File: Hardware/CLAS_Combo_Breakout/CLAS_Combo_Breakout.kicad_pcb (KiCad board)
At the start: 4 copper layers, 60 x 60 mm, 87 parts, among them J1 USB_C_Receptacle_USB2.0, J2 ZED, J3 NEO, J4 USB_C_Receptacle_USB2.0, J5 Conn_SMA, U1 USBLC6-2P6, U10 NT1191GEAE3S, U2 ZED-F9P, U3 NEO-D9C-00B, U4 USBLC6-2P6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

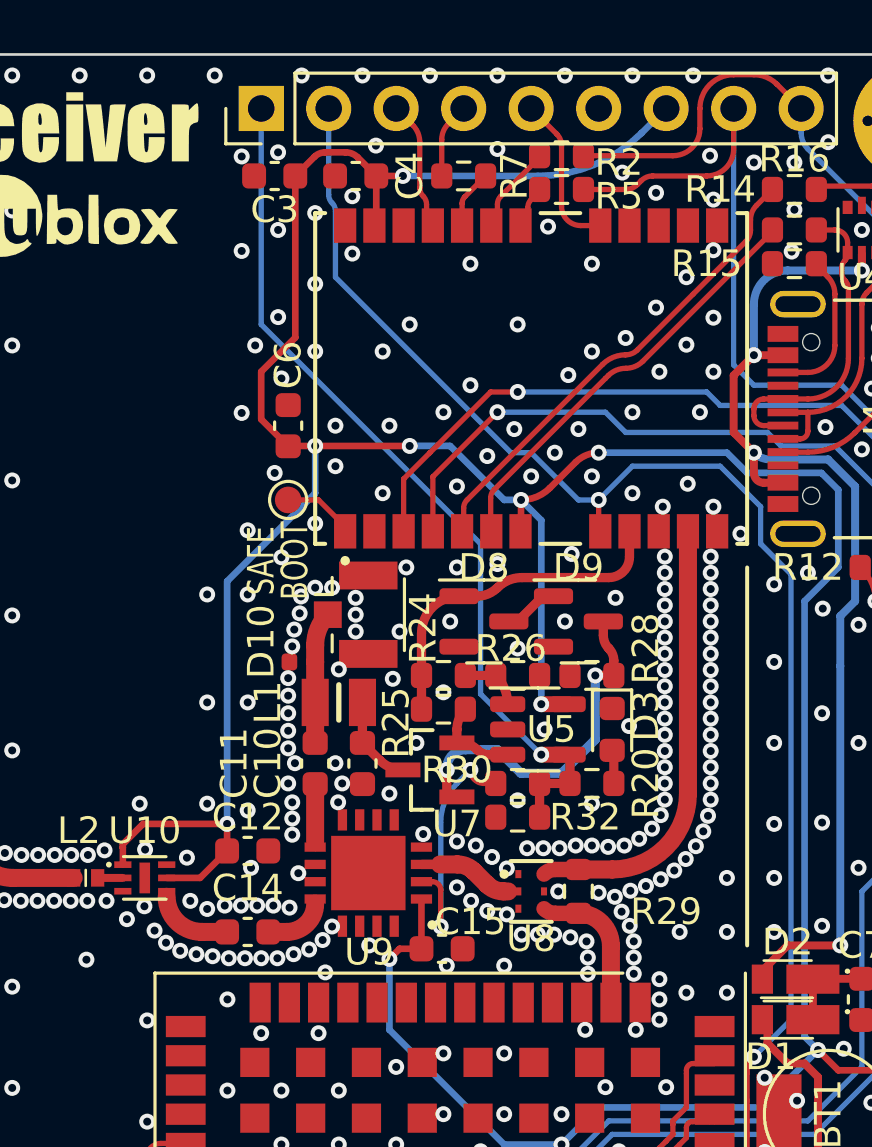
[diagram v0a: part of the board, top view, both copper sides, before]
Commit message: プルダウンRをプルアップRに変更、EANTのLEDを移動
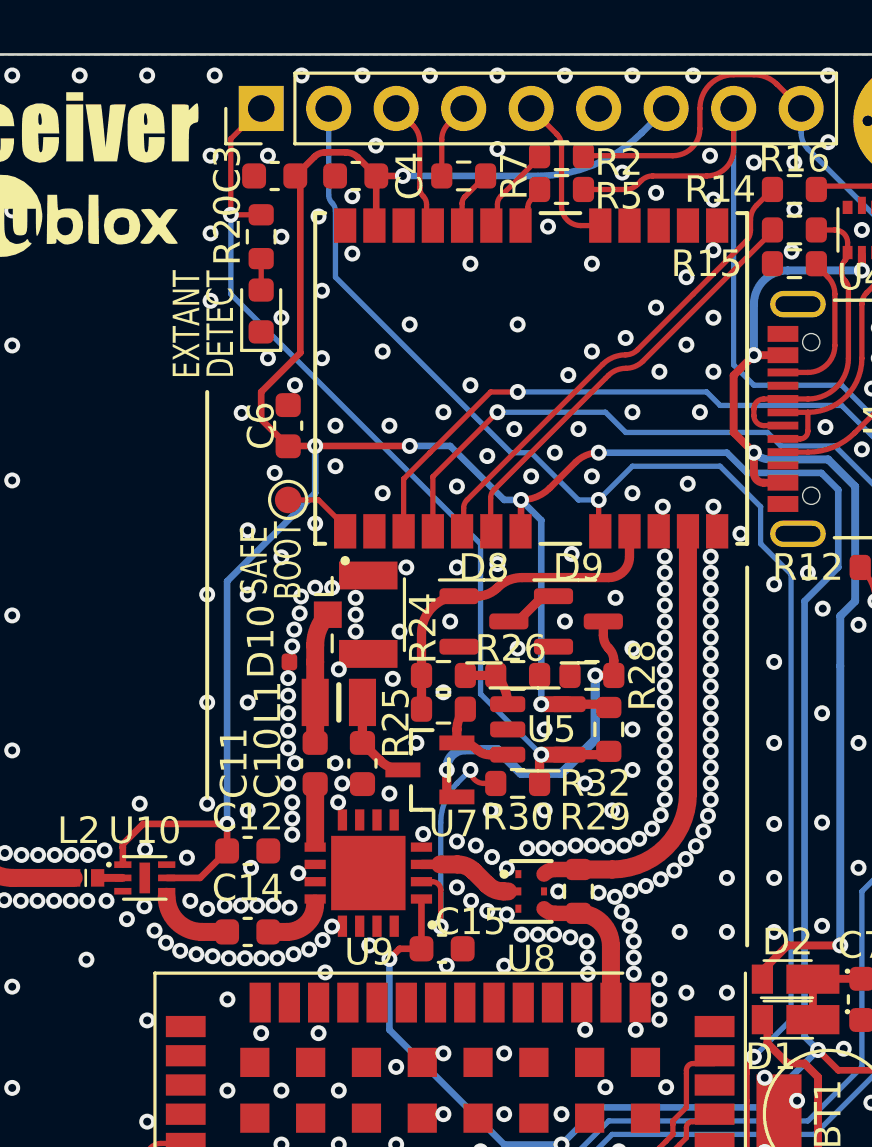
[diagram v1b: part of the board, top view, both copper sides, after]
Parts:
- moved R20 24.0 mm to (133.0, 96.9), turned to -90 degrees
- moved D3 20.6 mm to (133.0, 99.7), turned to 90 degrees
- moved R32 4.76 mm to (146.1, 115.4), turned to -90 degrees
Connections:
- R32 pad 1: GND -> +3.3V
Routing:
- net +3.3V: track 183.0 -> 184.8 mm
- net /EXTANT_DETECT: track 33.2 -> 34.5 mm, vias 1 -> 2
- net GND: vias 539 -> 544
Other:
- board text added: "DETECT"
- board text added: "EXTANT"

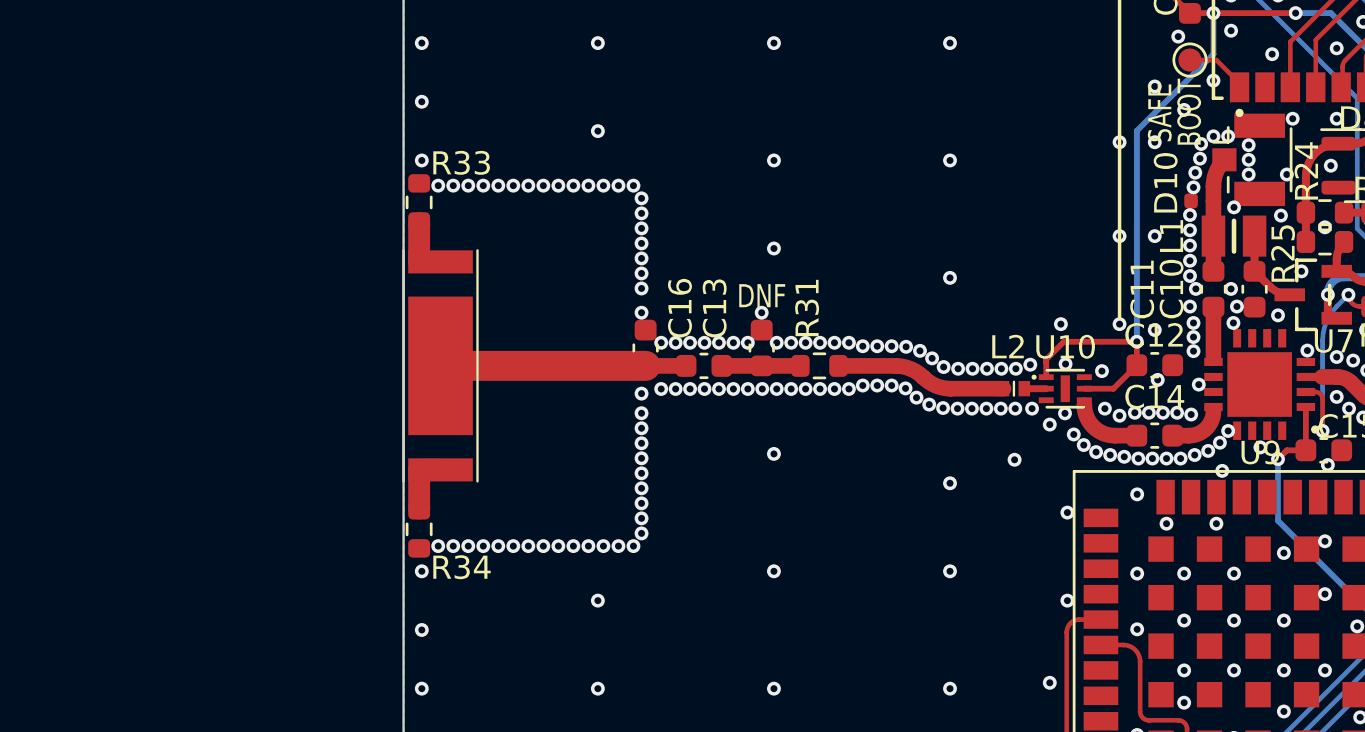
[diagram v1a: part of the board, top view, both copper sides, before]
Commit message: アンテナのFootprintをデータシートに準拠
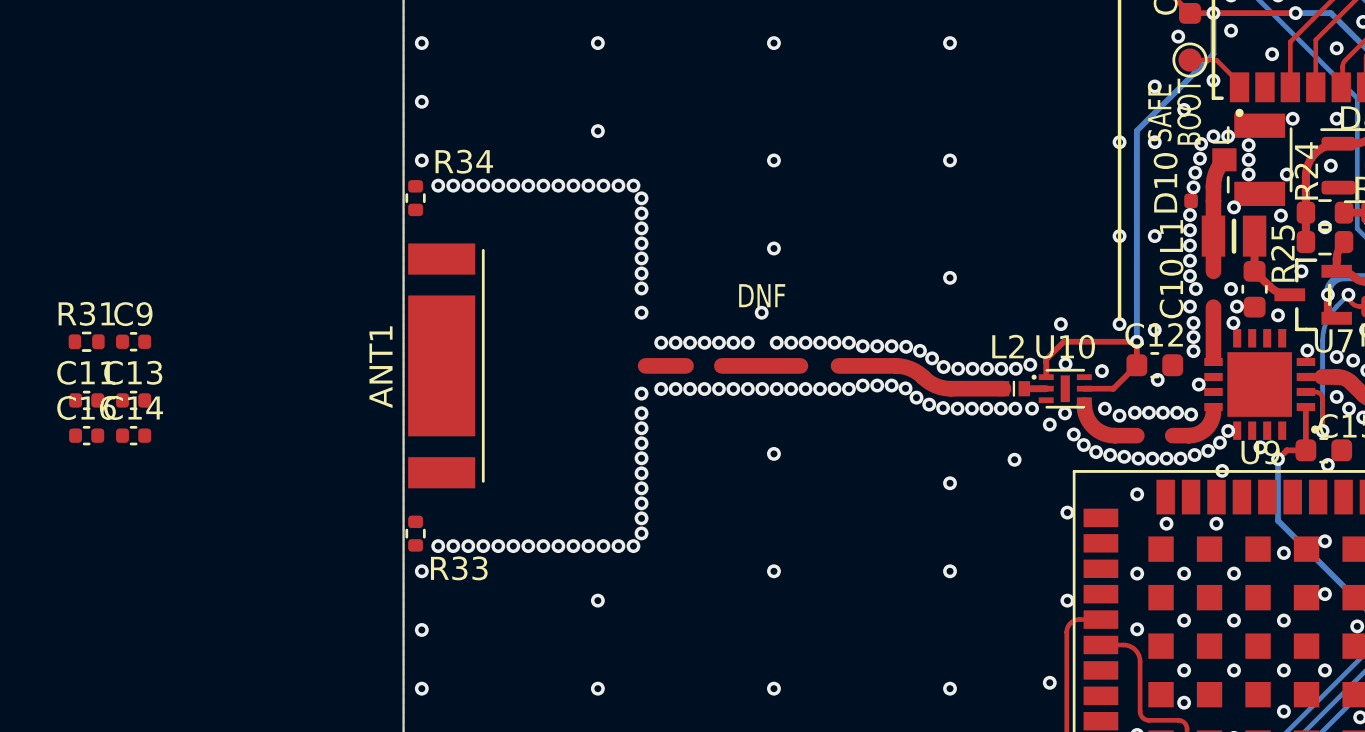
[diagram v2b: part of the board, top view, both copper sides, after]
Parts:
- ANT1: value GGBLA.125.A -> GGBLA125A
- C11, C13, C14, C16, C9: footprint Capacitor_SMD:C_0603_1608Metric -> Capacitor_SMD:C_0402_1005Metric
- R31, R33, R34: footprint Resistor_SMD:R_0603_1608Metric -> Resistor_SMD:R_0402_1005Metric
- moved C11 49.0 mm to (86.3, 121.5), turned to 0 degrees
- moved C14 44.2 mm to (88.3, 123.0), turned to 0 degrees
- moved R31 31.7 mm to (86.3, 119.0)
- moved C9 27.2 mm to (88.3, 119.0), turned to 0 degrees
- moved C13 24.7 mm to (88.3, 121.5)
- moved C16 24.5 mm to (86.3, 123.0), turned to 0 degrees
- moved R33 14.3 mm to (100.5, 127.3), turned to -90 degrees
- moved R34 14.3 mm to (100.5, 112.7), turned to 90 degrees
- moved ANT1 0.05 mm to (101.7, 120.0), turned to 90 degrees
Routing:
- net Net-(ANT1-Pad1): track 10.6 -> 1.75 mm
- net Net-(ANT1-Pad3): track 2.60 -> 0.00 mm
- net Net-(ANT1-Pad2): track 2.60 -> 0.00 mm

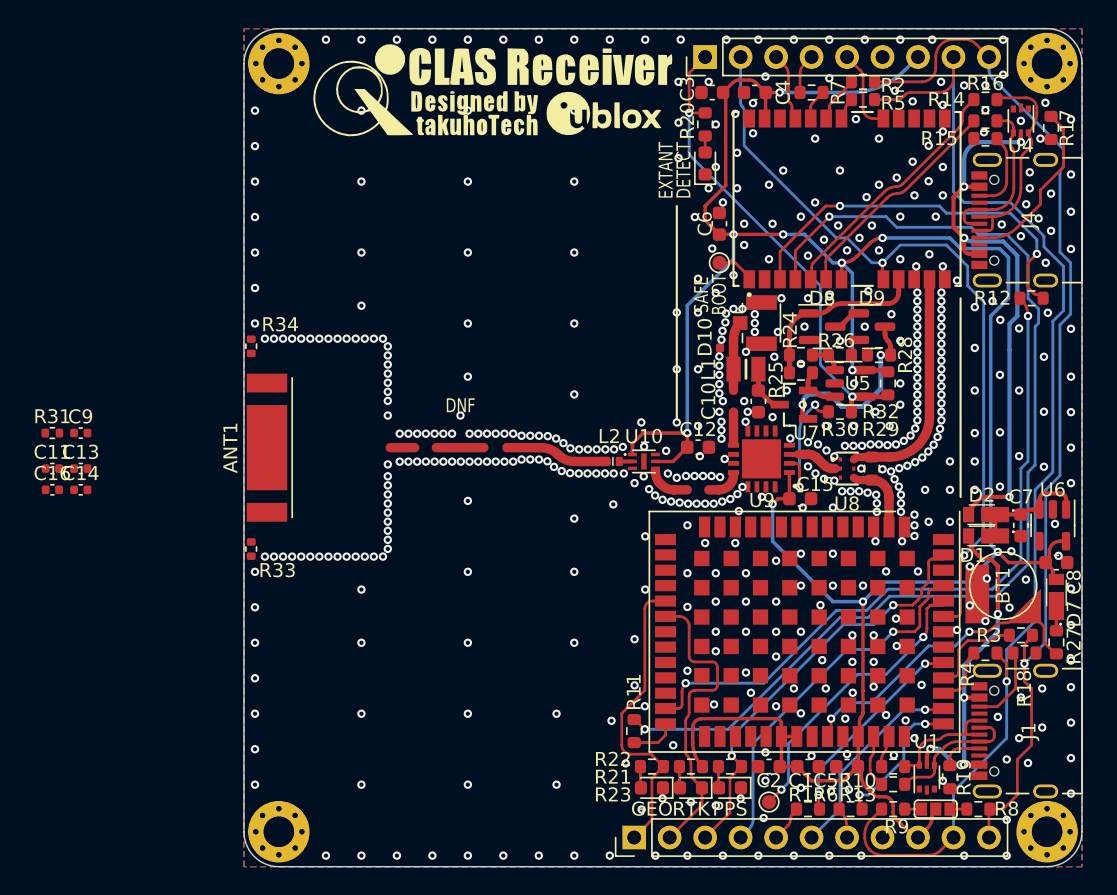
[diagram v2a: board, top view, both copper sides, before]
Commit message: トランジスタの記号をQに変更、REFを整理
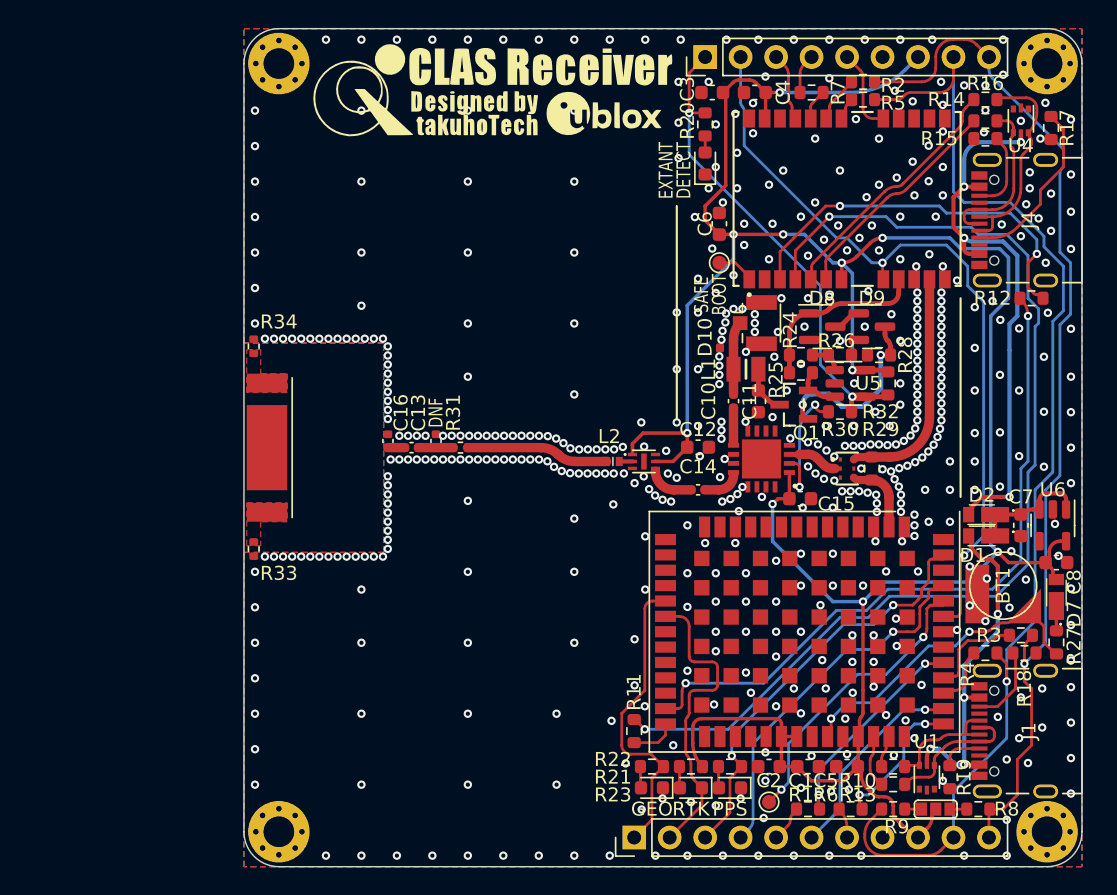
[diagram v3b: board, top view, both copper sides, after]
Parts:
- ANT1: value GGBLA125A -> GGBLA.125.A
- moved C11 49.0 mm to (135.1, 116.7), turned to -90 degrees
- moved C14 44.2 mm to (132.5, 123.0), turned to 180 degrees
- moved R31 29.2 mm to (115.5, 120.0)
- moved C9 25.4 mm to (113.8, 119.5), turned to 90 degrees
- moved C16 24.3 mm to (110.3, 119.5), turned to 90 degrees
- moved C13 23.7 mm to (112.0, 120.0)
- moved R33 0.18 mm to (100.7, 127.3)
- moved R34 0.18 mm to (100.7, 112.7)
- renumbered U7 to Q1, U10 to U7, U9 to U8, U8 to U9
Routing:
- net Net-(L2-Pad1): track 7.39 -> 10.2 mm
- net Net-(C13-Pad2): track 3.40 -> 2.51 mm
- net Net-(ANT1-Pad1): track 1.75 -> 1.21 mm
- net GND: vias 544 -> 530
- added copper zone on F.Cu, net Net-(ANT1-Pad2)
- added copper zone on F.Cu, net Net-(ANT1-Pad3)

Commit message: アンテナ伝送路0.678mmバージョン
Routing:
- net Net-(ANT1-Pad1): track 1.21 -> 9.87 mm
- net GND: vias 530 -> 548

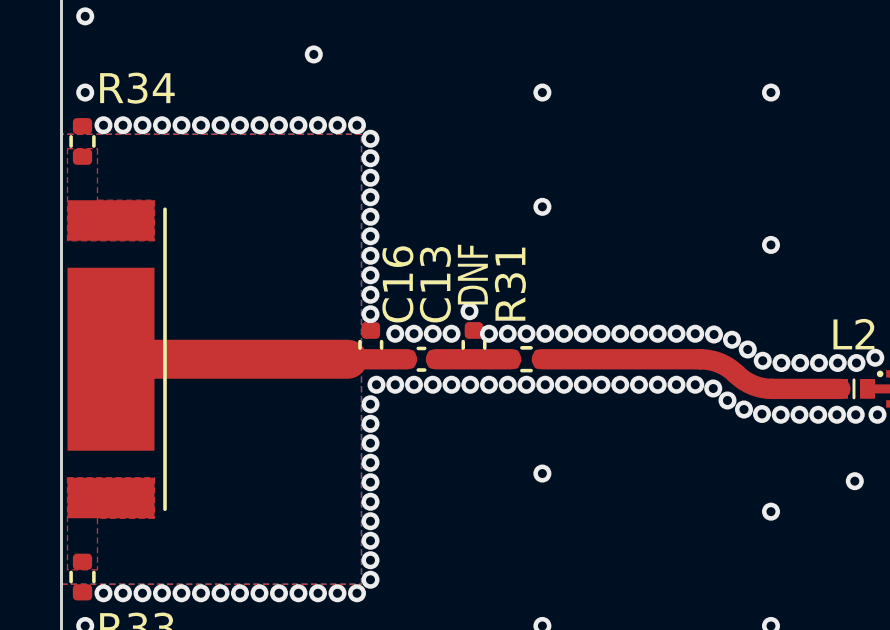
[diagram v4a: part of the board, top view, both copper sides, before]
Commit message: アンテナのマッチング回路を再設計
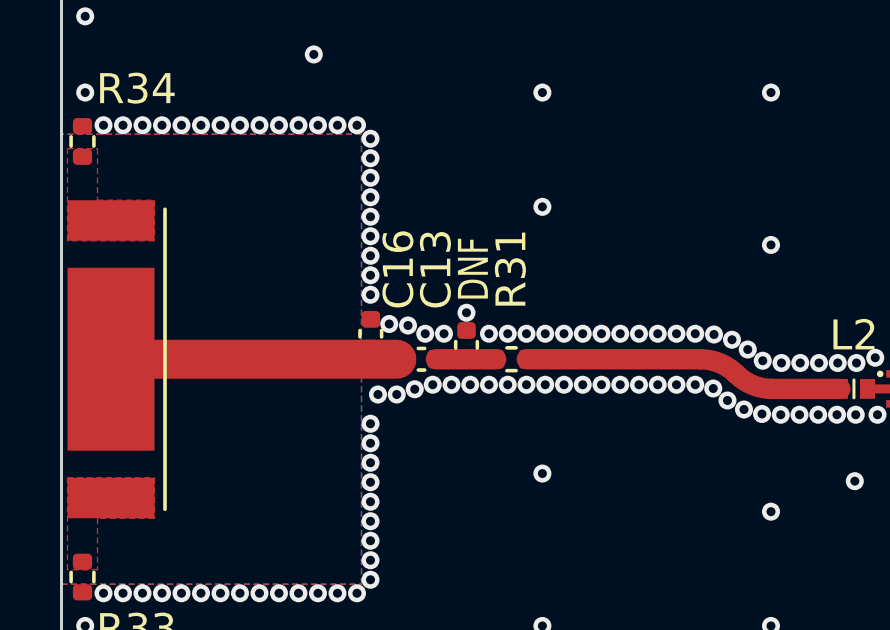
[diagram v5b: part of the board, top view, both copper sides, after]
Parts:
- moved R31 0.50 mm to (115.0, 120.0)
- moved C16 0.37 mm to (110.3, 119.2)
- moved C9 0.25 mm to (113.5, 119.5)
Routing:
- net Net-(L2-Pad1): track 10.2 -> 10.7 mm
- net Net-(C13-Pad2): track 2.51 -> 2.01 mm
- net GND: vias 548 -> 546

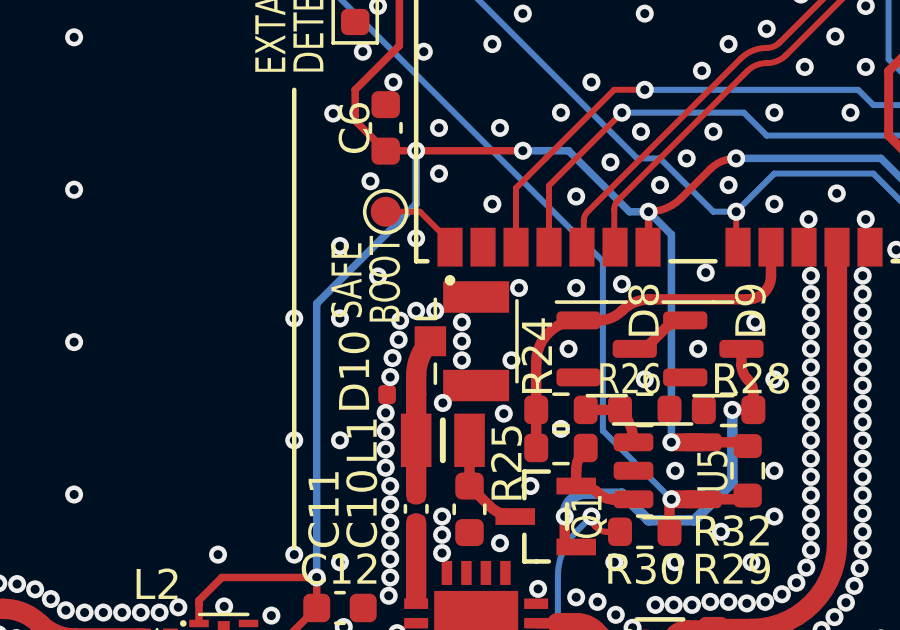
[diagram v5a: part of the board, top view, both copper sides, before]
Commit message: MMCXのフットプリントを作成　ピン表示のシルクの位置調整
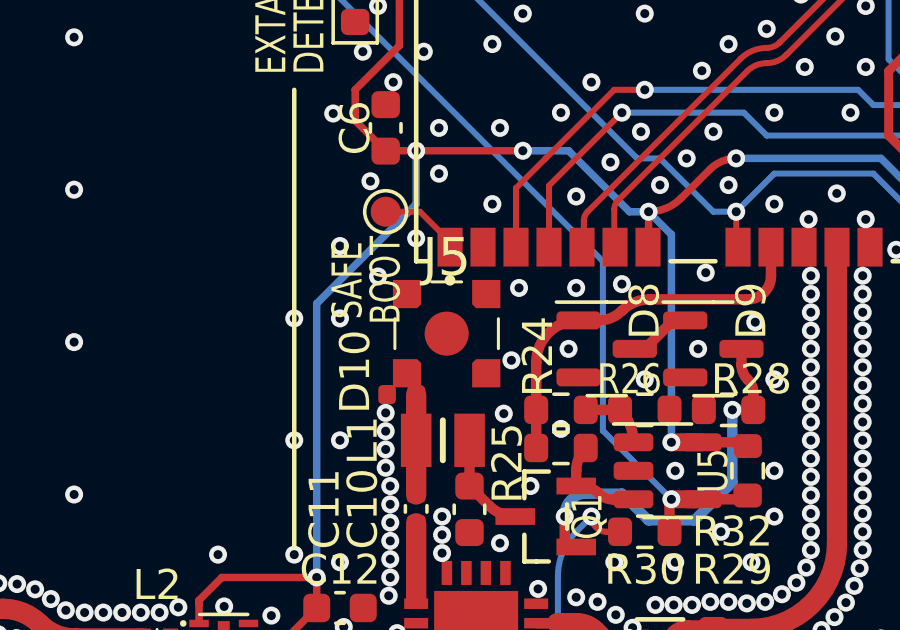
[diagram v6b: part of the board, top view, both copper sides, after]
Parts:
- J5: value Conn_SMA -> Conn_Coaxial; footprint Connector_Coaxial:U.FL_Hirose_U.FL-R-SMT-1_Vertical -> Connector_Coaxial_extlib:0734152063
- moved J5 0.57 mm to (136.1, 110.8)
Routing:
- net Net-(C11-Pad1): track 5.23 -> 3.33 mm
- net GND: vias 546 -> 536
